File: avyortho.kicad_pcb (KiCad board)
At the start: 2 copper layers, 230 x 77.2 mm, 100 parts, among them SW1 SW_Push_45deg, SW10 SW_Push_45deg, SW11 SW_Push_45deg, SW12 SW_Push_45deg, SW13 SW_Push_45deg, SW14 SW_Push_45deg, SW15 SW_Push_45deg, SW16 SW_Push_45deg, SW17 SW_Push_45deg, SW18 SW_Push_45deg, SW19 SW_Push_45deg, SW2 SW_Push_45deg, SW20 SW_Push_45deg, SW21 SW_Push_45deg, SW22 SW_Push_45deg, SW23 SW_Push_45deg, SW24 SW_Push_45deg, SW25 SW_Push_45deg, SW26 SW_Push_45deg, SW27 SW_Push_45deg, SW28 SW_Push_45deg, SW29 SW_Push_45deg, SW3 SW_Push_45deg, SW30 SW_Push_45deg, SW31 SW_Push_45deg, SW32 SW_Push_45deg, SW33 SW_Push_45deg, SW34 SW_Push_45deg, SW35 SW_Push_45deg, SW36 SW_Push_45deg, SW37 SW_Push_45deg, SW38 SW_Push_45deg, SW39 SW_Push_45deg, SW4 SW_Push_45deg, SW40 SW_Push_45deg, SW41 SW_Push_45deg, SW42 SW_Push_45deg, SW43 SW_Push_45deg, SW45 SW_Push_45deg, SW46 SW_Push_45deg, SW47 SW_Push_45deg, SW48 SW_Push_45deg, SW5 SW_Push_45deg, SW6 SW_Push_45deg, SW7 SW_Push_45deg, SW8 SW_Push_45deg, SW9 SW_Push_45deg, U3 XIAO-nRF52840-Plus-SMD

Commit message: route pcb and add silkscreen
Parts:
- added G***: LOGO, footprints:yoyo-orpheus-silkscreen, B.Cu at (63.8, 75.8)
- added G***: LOGO, footprints:neocat-silkscreen, B.Cu at (40.2, 80.6)
- moved D1 3.09 mm to (51.0, 47.5)
- moved U3 1.73 mm to (39.7, 39.1)
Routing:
- net /COL11: track 57.1 -> 321.5 mm, vias 0 -> 13
- net /COL8: track 19.0 -> 263.7 mm, vias 0 -> 16
- net /COL10: track 57.1 -> 299.8 mm, vias 0 -> 1
- net /COL9: track 57.1 -> 284.6 mm, vias 0 -> 1
- net /COL7: track 39.0 -> 241.7 mm, vias 0 -> 3
- net /COL6: track 38.1 -> 159.0 mm, vias 0 -> 11
- net /COL5: track 59.6 -> 156.5 mm, vias 0 -> 9
- net /COL4: track 57.1 -> 133.6 mm, vias 0 -> 7
- net /ROW3: track 209.6 -> 279.6 mm, vias 0 -> 6
- net /ROW2: track 190.5 -> 258.2 mm, vias 0 -> 2
- net /ROW1: track 190.5 -> 252.0 mm, vias 0 -> 8
- net /COL3: track 57.1 -> 117.1 mm, vias 0 -> 2
- net /VBAT_SNS: track 0.00 -> 33.2 mm, vias 0 -> 5
- net /COL2: track 57.1 -> 89.1 mm, vias 0 -> 3
- net Net-(D1-A): track 0.00 -> 25.2 mm, vias 0 -> 1
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- added copper zone on B.Cu, net GND
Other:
- board size 230 x 77.2 mm -> 230 x 78 mm
- board text added: "made by avy (avycado13), 2026"

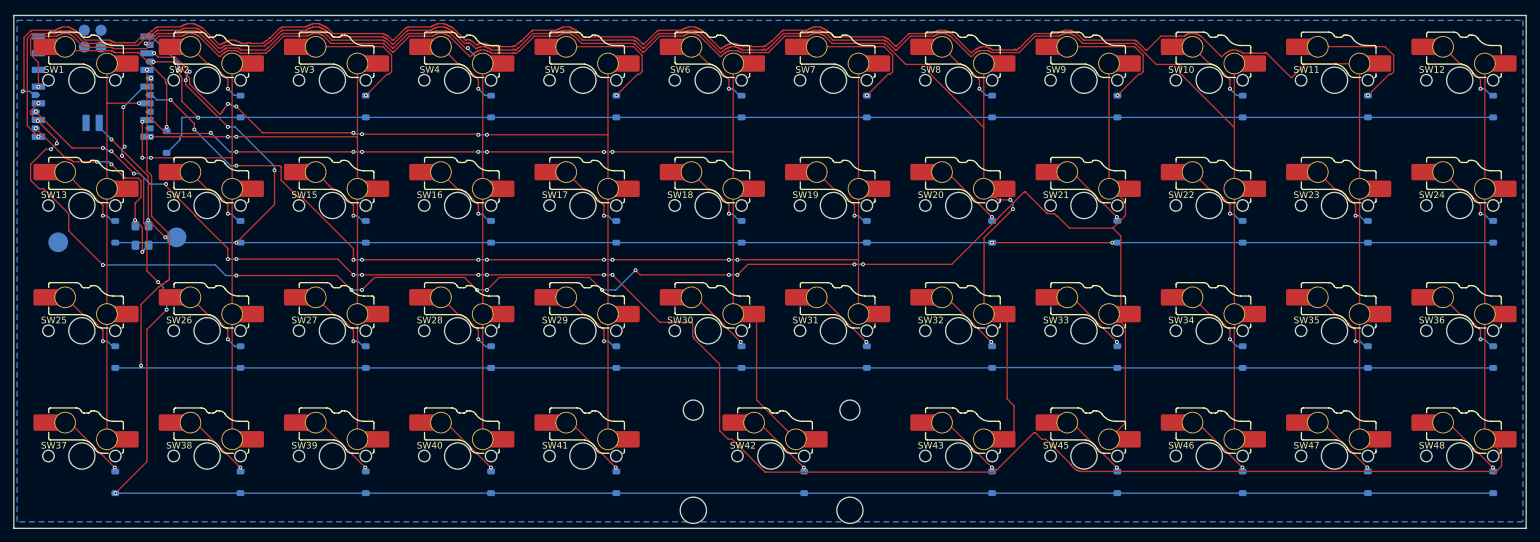
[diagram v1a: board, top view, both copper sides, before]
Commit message: switch sockets to Kalih CPG151101S11-16 because available at lcsc
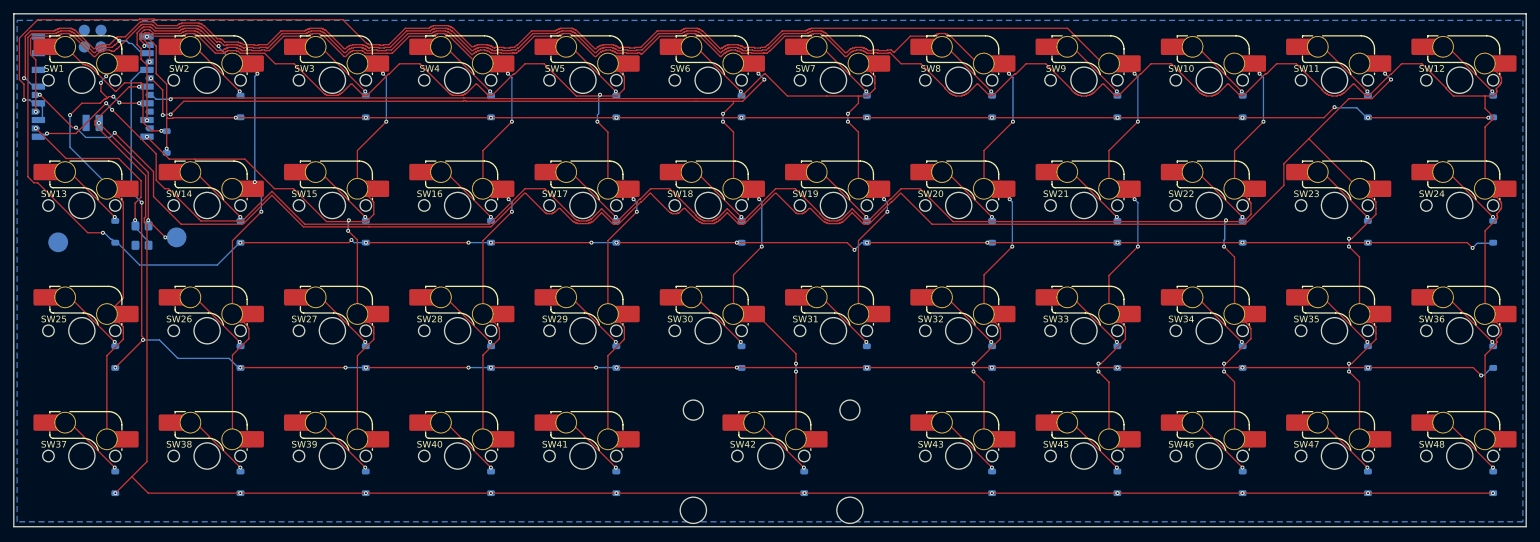
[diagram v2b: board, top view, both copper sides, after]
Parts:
- SW1, SW10, SW11, SW12, SW13, SW14, SW15, SW16, SW17, SW18, SW19, SW2, SW20, SW21, SW22, SW23, SW24, SW25, SW26, SW27, SW28, SW29, SW3, SW30, SW31, SW32, SW33, SW34, SW35, SW36, SW37, SW38, SW39, SW4, SW40, SW41, SW42, SW43, SW45, SW46, SW47, SW48, SW5, SW6, SW7, SW8, SW9: footprint PCM_marbastlib-mx:SW_MX_HS_KS-2P02B01-01_1u -> PCM_marbastlib-mx:SW_MX_HS_CPG151101S11_1u
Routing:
- net /COL4: track 133.6 -> 160.8 mm, vias 7 -> 5
- net /COL11: track 321.5 -> 346.6 mm, vias 13 -> 1
- net /ROW1: track 252.0 -> 275.7 mm, vias 8 -> 17
- net /COL1: track 77.1 -> 100.0 mm, vias 3 -> 5
- net /COL3: track 117.1 -> 135.3 mm, vias 2 -> 5
- net /COL2: track 89.1 -> 105.9 mm, vias 3 -> 5
- net /COL10: track 299.8 -> 316.5 mm, vias 1 -> 9
- net /COL0: track 63.2 -> 77.8 mm, vias 1 -> 6
- net /COL5: track 156.5 -> 168.1 mm, vias 9 -> 11
- net /COL7: track 241.7 -> 252.1 mm, vias 3 -> 7
- net Net-(D9-A): track 19.9 -> 11.0 mm
- net Net-(D11-A): track 19.9 -> 11.0 mm
- net Net-(D7-A): track 19.9 -> 11.0 mm
- net Net-(D3-A): track 19.9 -> 11.0 mm
- net Net-(D5-A): track 19.9 -> 11.0 mm
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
